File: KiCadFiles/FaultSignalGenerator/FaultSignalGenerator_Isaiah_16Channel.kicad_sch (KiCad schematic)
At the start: 1 part

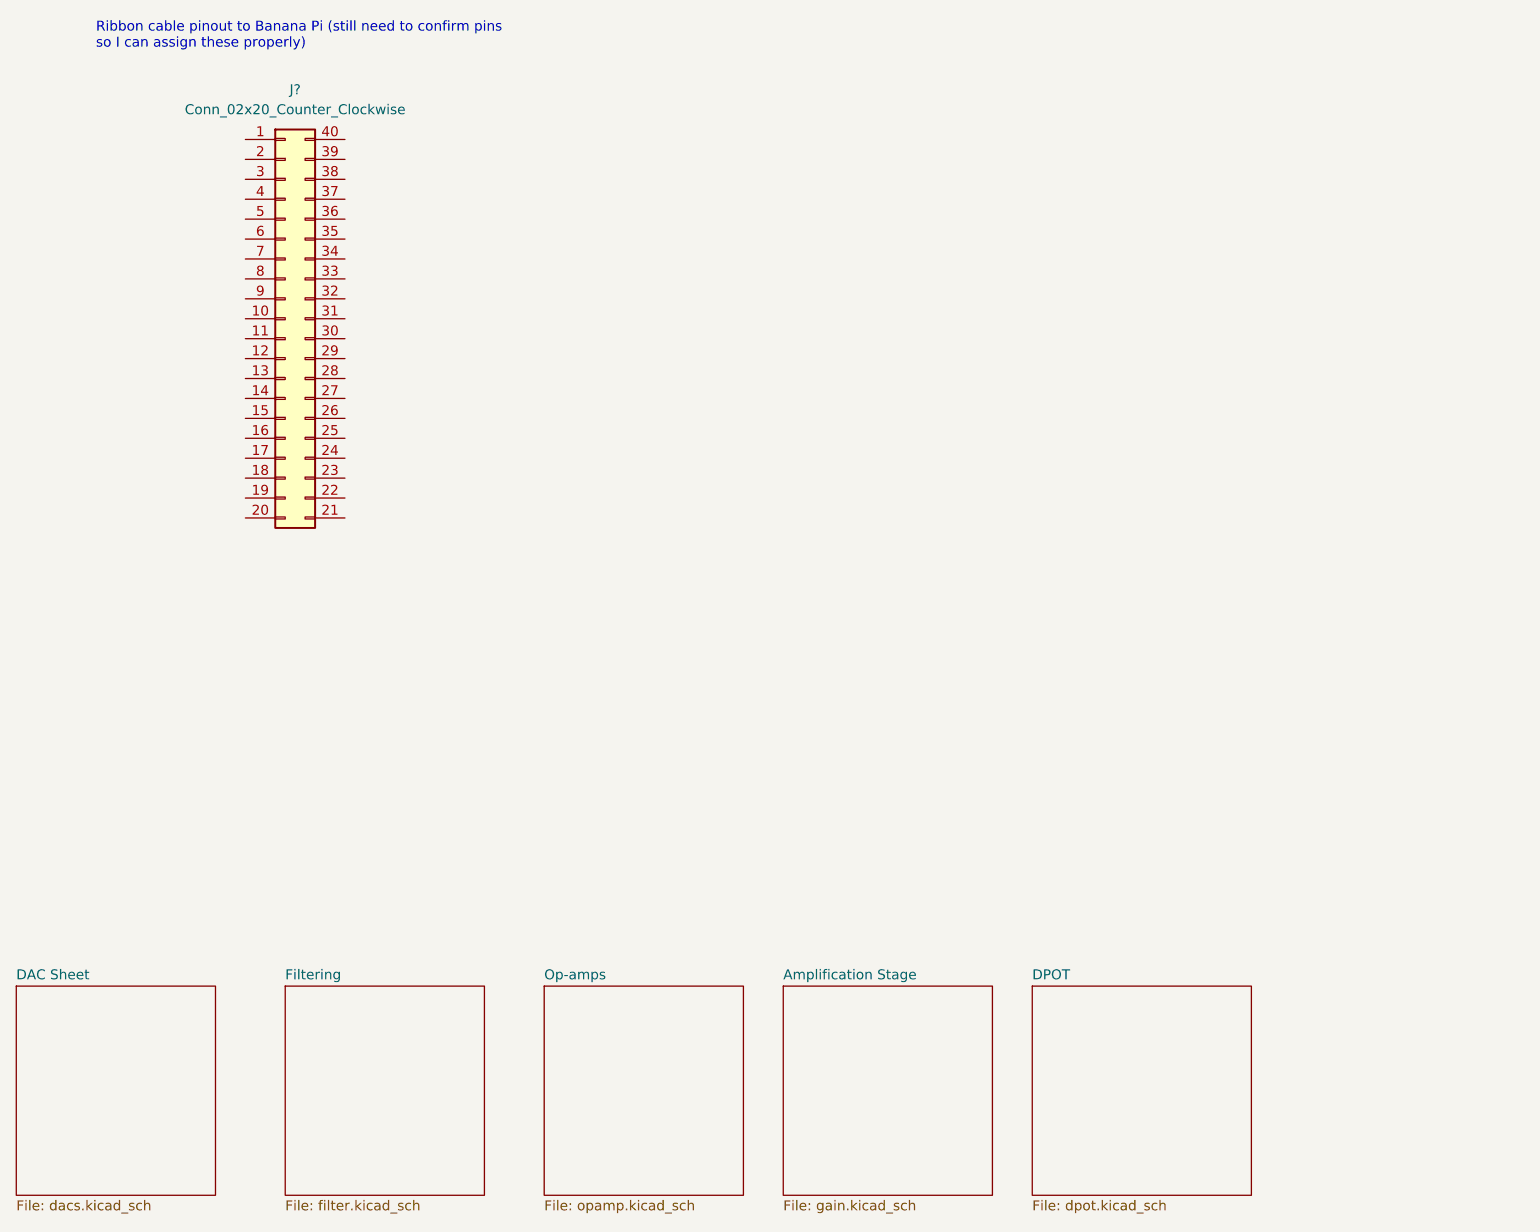
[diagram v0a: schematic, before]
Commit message: Pi Connection and LED Array connection
Added I2C connections from Pi to the rest of the PCB using the Pi schema. Also included LED status array connector to board, presuming we use a 2x16 pin header. Each LED is just powered by basic GPIO.
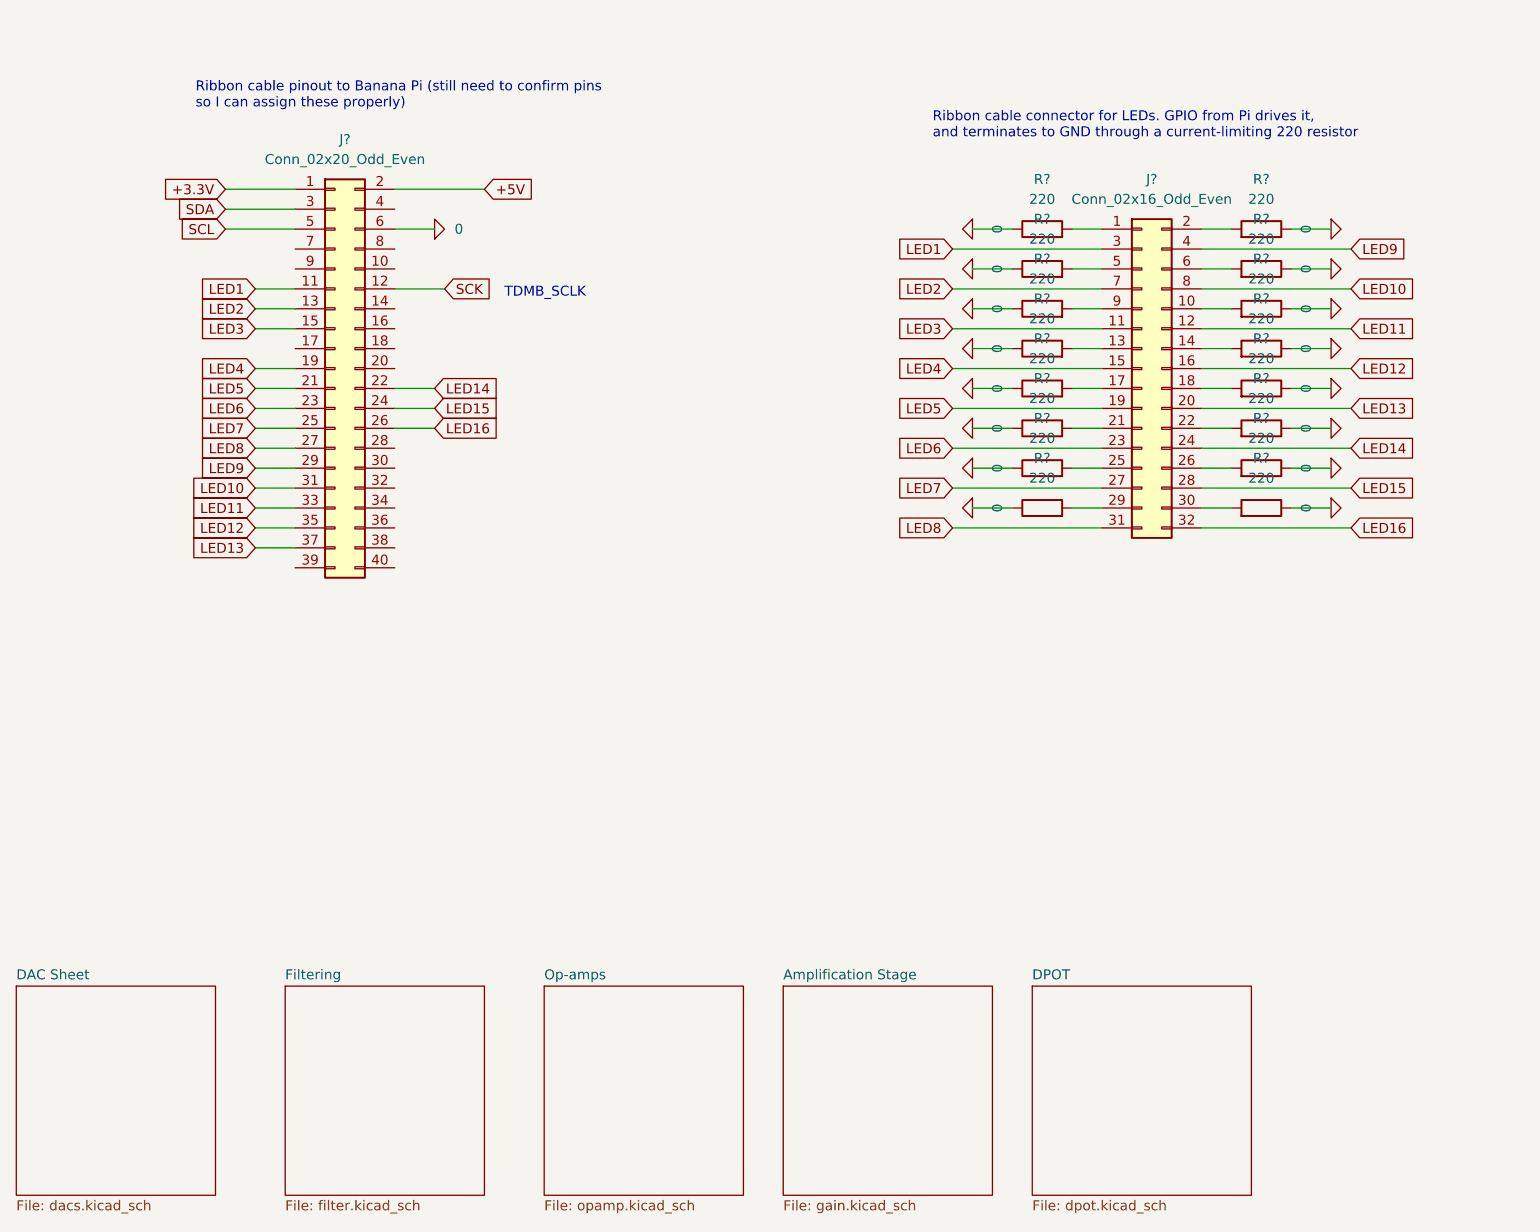
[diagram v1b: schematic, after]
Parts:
- removed J?: Conn_02x20_Counter_Clockwise, Connector_JAE:JAE_LY20-40P-DT1_2x20_P2.00mm_Vertical, symbol Connector_Generic:Conn_02x20_Counter_Clockwise
- added J?: Conn_02x20_Odd_Even, symbol Connector_Generic:Conn_02x20_Odd_Even
- added J?: Conn_02x16_Odd_Even, symbol Connector_Generic:Conn_02x16_Odd_Even
- added R? (x16): 220, Resistor_SMD:R_0603_1608Metric_Pad0.98x0.95mm_HandSolder, symbol Device:R
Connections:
- new net: J?.6 (Pin_6), R?.2
- new net: J?.25 (Pin_25), R?.2
- new net: J?.18 (Pin_18), R?.2
- new net: J?.22 (Pin_22), R?.2
- new net: J?.26 (Pin_26), R?.2
- new net: J?.5 (Pin_5), R?.2
- new net: J?.29 (Pin_29), R?.2
- new net: J?.13 (Pin_13), R?.2
- new net: J?.9 (Pin_9), R?.2
- new net: J?.10 (Pin_10), R?.2
- new net: J?.30 (Pin_30), R?.2
- new net: J?.14 (Pin_14), R?.2
- new net: J?.1 (Pin_1), R?.2
- new net: J?.17 (Pin_17), R?.2
- new net: J?.2 (Pin_2), R?.2
- new net: J?.21 (Pin_21), R?.2
- new net +3.3V: J?.1 (Pin_1)
- new net +5V: J?.2 (Pin_2)
- new net 0: J?.6 (Pin_6), R?.1, R?.1, R?.1, R?.1, R?.1, R?.1, R?.1, R?.1, R?.1, R?.1, R?.1, R?.1, R?.1, R?.1, R?.1, R?.1
- new net LED1: J?.11 (Pin_11), J?.3 (Pin_3)
- new net LED10: J?.31 (Pin_31), J?.8 (Pin_8)
- new net LED11: J?.12 (Pin_12), J?.33 (Pin_33)
- new net LED12: J?.16 (Pin_16), J?.35 (Pin_35)
- new net LED13: J?.20 (Pin_20), J?.37 (Pin_37)
- new net LED14: J?.22 (Pin_22), J?.24 (Pin_24)
- new net LED15: J?.24 (Pin_24), J?.28 (Pin_28)
- new net LED16: J?.26 (Pin_26), J?.32 (Pin_32)
- new net LED2: J?.13 (Pin_13), J?.7 (Pin_7)
- new net LED3: J?.11 (Pin_11), J?.15 (Pin_15)
- new net LED4: J?.15 (Pin_15), J?.19 (Pin_19)
- new net LED5: J?.19 (Pin_19), J?.21 (Pin_21)
- new net LED6: J?.23 (Pin_23), J?.23 (Pin_23)
- new net LED7: J?.25 (Pin_25), J?.27 (Pin_27)
- new net LED8: J?.27 (Pin_27), J?.31 (Pin_31)
- new net LED9: J?.29 (Pin_29), J?.4 (Pin_4)
- new net SCK: J?.12 (Pin_12)
- new net SCL: J?.5 (Pin_5)
- new net SDA: J?.3 (Pin_3)
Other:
- note added: "Ribbon cable connector for LEDs. GPIO from Pi drives it, and terminates to GND through a current-limiting 220 resistor"
- note added: "TDMB_SCLK"

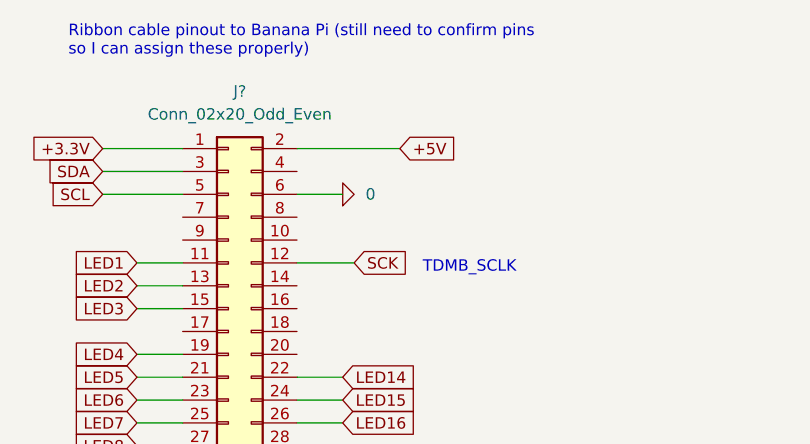
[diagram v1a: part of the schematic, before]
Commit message: Added both 5V GPIO Pin labels
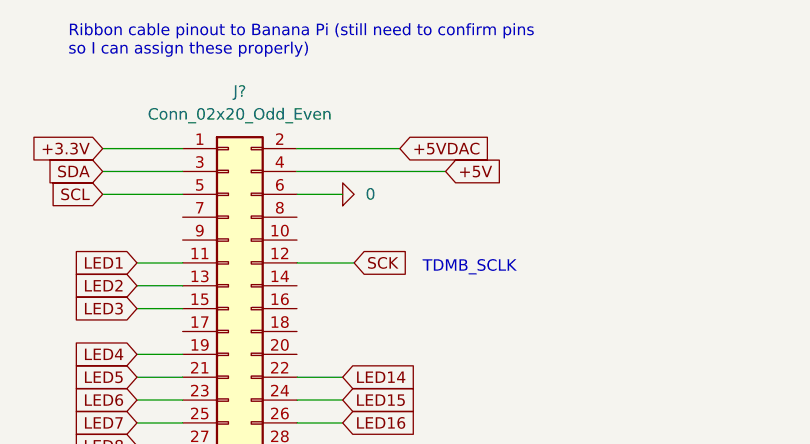
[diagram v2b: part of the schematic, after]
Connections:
- net +5V: now also J?.4 (Pin_4); no longer J?.2 (Pin_2)
- new net +5VDAC: J?.2 (Pin_2)
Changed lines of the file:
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@@
+    (stroke (width 0) (type default) (color 0 0 0 0))
+  )
+  (wire (pts (xy 81.28 59.69) (xy 64.77 59.69))
     (stroke (width 0) (type default) (color 0 0 0 0))
   )
@@
     )
   )
-  (global_label "+5V" (shape input) (at 76.2 57.15 0) (fields_autoplaced)
+  (global_label "+5VDAC" (shape input) (at 76.2 57.15 0) (fields_autoplaced)
     (effects (font (size 1.27 1.27)) (justify left))
-    (property "Intersheet References" "${INTERSHEET_REFS}" (id 0) (at 82.4836 57.0706 0)
+    (property "Intersheet References" "${INTERSHEET_REFS}" (id 0) (at 86.1121 57.0706 0)
       (effects (font (size 1.27 1.27)) (justify left) hide)
     )
@@
     )
   )
+  (global_label "+5V" (shape input) (at 81.28 59.69 0) (fields_autoplaced)
+    (effects (font (size 1.27 1.27)) (justify left))
+    (property "Intersheet References" "${INTERSHEET_REFS}" (id 0) (at 87.5636 59.6106 0)
+      (effects (font (size 1.27 1.27)) (justify left) hide)
+    )
+  )

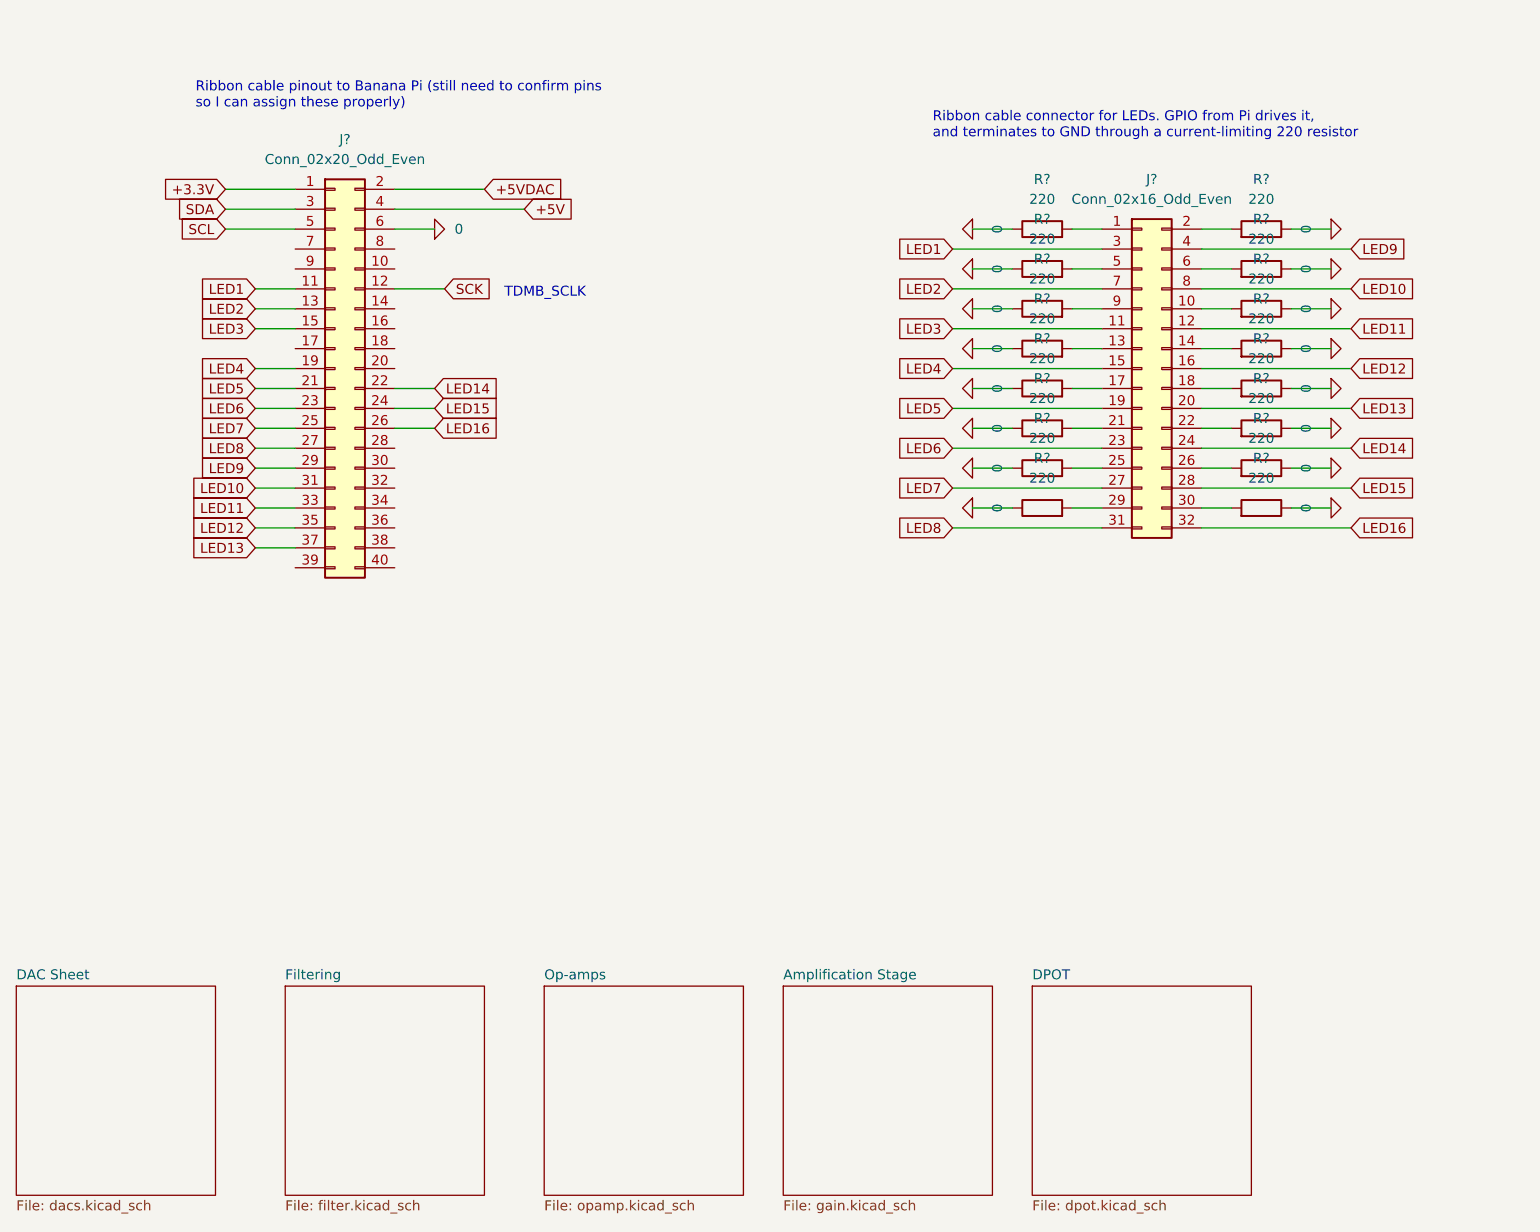
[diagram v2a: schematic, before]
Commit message: Finish schematic, start on PCB
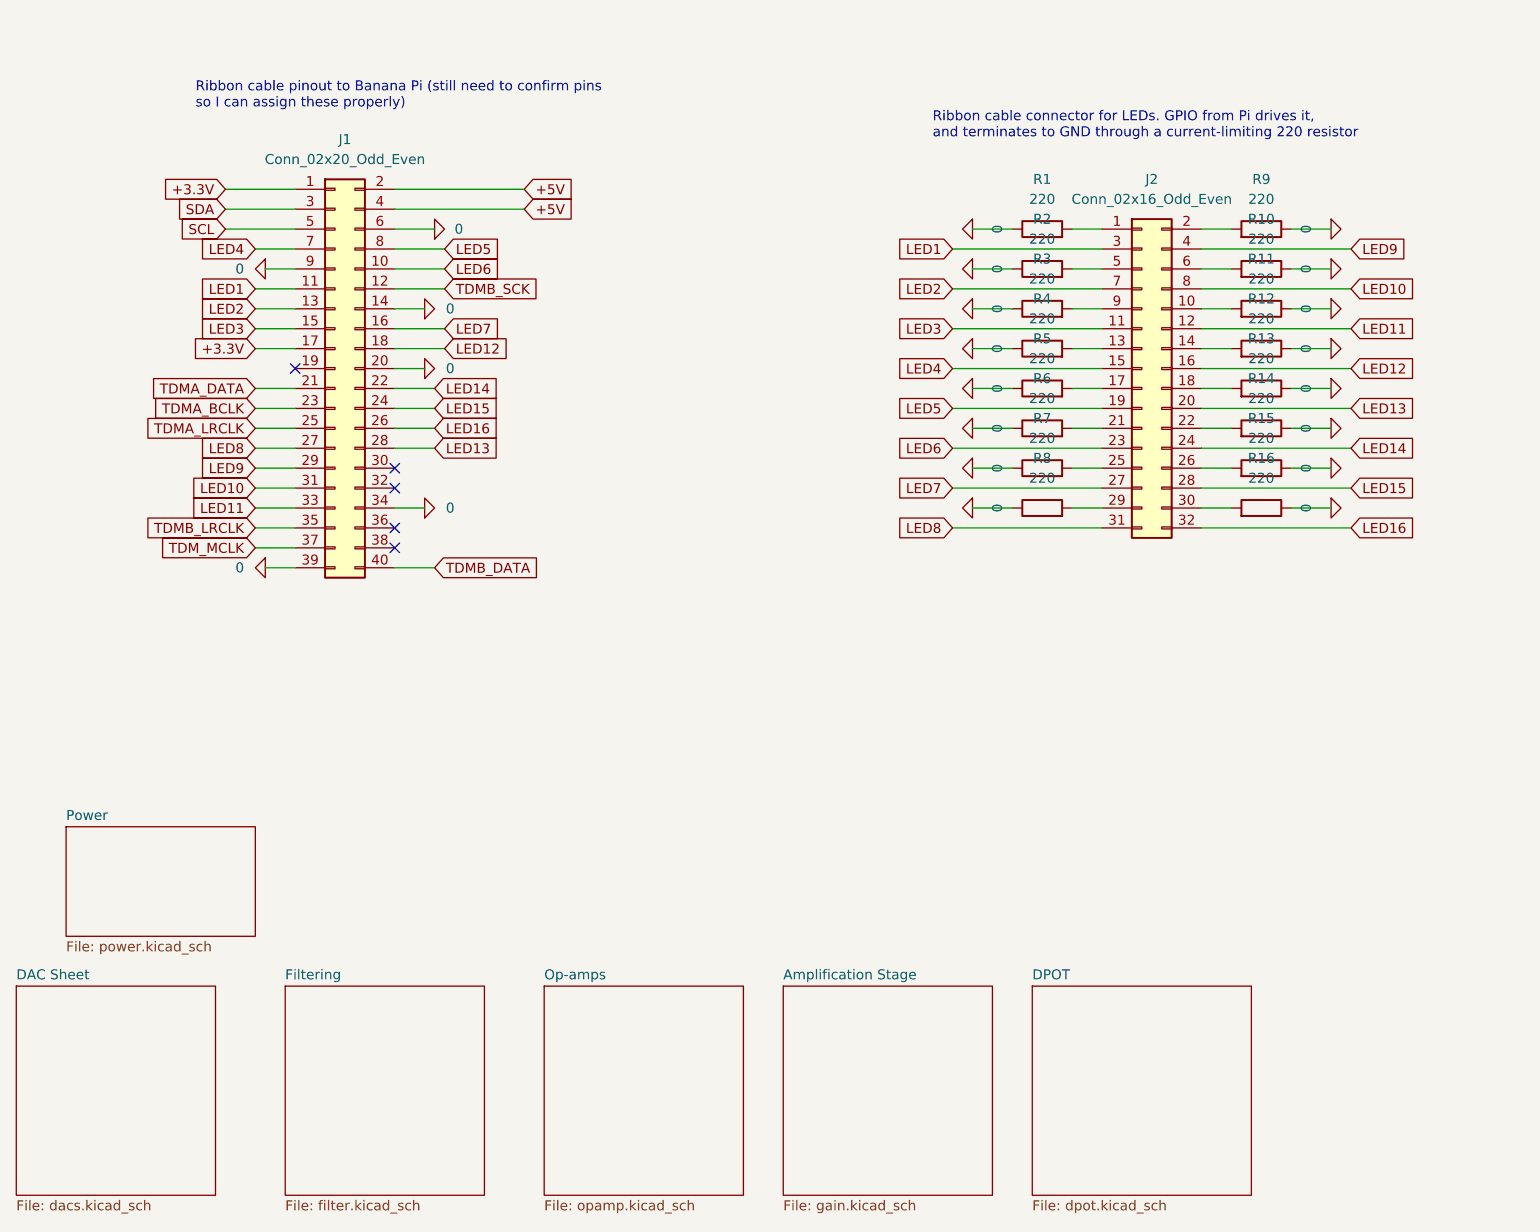
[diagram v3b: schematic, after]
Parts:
- J1: renamed from J?; footprint (none) -> Connector_PinSocket_2.54mm:PinSocket_2x20_P2.54mm_Vertical_SMD
- J2: renamed from J?; footprint (none) -> Connector_PinSocket_2.54mm:PinSocket_2x16_P2.54mm_Vertical_SMD
- R1, R10, R11, R12, R13, R14, R15, R16, R2, R3, R4, R5, R6, R7, R8, R9: renamed from R?; footprint Resistor_SMD:R_0603_1608Metric_Pad0.98x0.95mm_HandSolder -> Resistor_SMD:R_1206_3216Metric; Spice_Model 6.2k -> (none); Spice_Netlist_Enabled Y -> (none); Spice_Primitive R -> (none)
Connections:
- net +5VDAC is gone; now on net +5V: J1.2 (Pin_2)
- net +3.3V: now also J1.17 (Pin_17)
- net 0: now also J1.14 (Pin_14), J1.20 (Pin_20), J1.34 (Pin_34), J1.39 (Pin_39), J1.9 (Pin_9)
- net LED12: now also J1.18 (Pin_18); no longer J1.35 (Pin_35)
- net LED13: now also J1.28 (Pin_28); no longer J1.37 (Pin_37)
- net LED4: now also J1.7 (Pin_7); no longer J1.19 (Pin_19)
- net LED5: now also J1.8 (Pin_8); no longer J1.21 (Pin_21)
- net LED6: now also J1.10 (Pin_10); no longer J1.23 (Pin_23)
- net LED7: now also J1.16 (Pin_16); no longer J1.25 (Pin_25)
- net TDMB_DATA: now reaches J1.40 (Pin_40)
- net SCK renamed TDMB_SCK
- new net TDMA_BCLK: J1.23 (Pin_23)
- new net TDMA_DATA: J1.21 (Pin_21)
- new net TDMA_LRCLK: J1.25 (Pin_25)
- new net TDMB_LRCLK: J1.35 (Pin_35)
- new net TDM_MCLK: J1.37 (Pin_37)
- no-connect marks 0 -> 5
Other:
- added sheet Power (power.kicad_sch)
- note removed: "TDMB_SCLK"
